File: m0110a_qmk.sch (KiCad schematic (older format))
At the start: 174 parts, among them J1 USB_B_Mini, J2 AVR-ISP-6, U1 ATmega32A-PU, Y1 Resonator

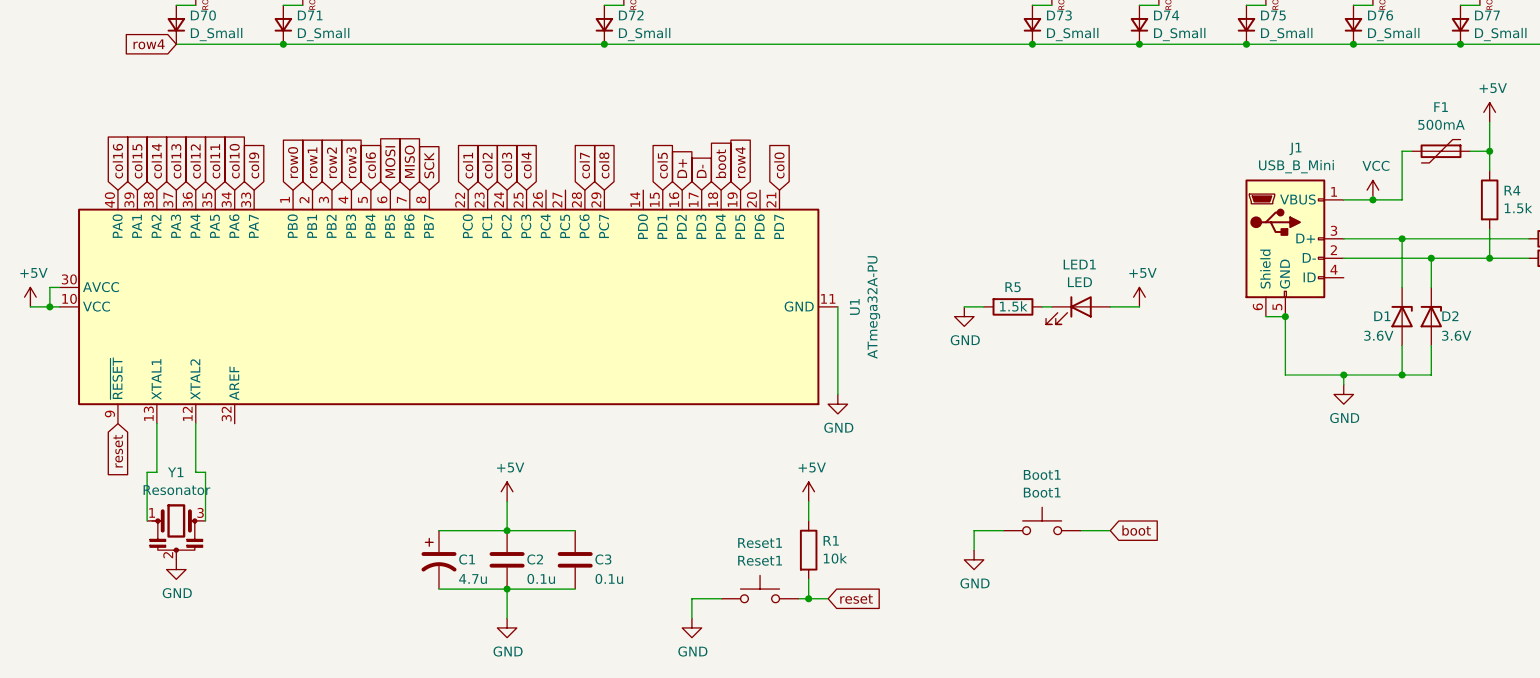
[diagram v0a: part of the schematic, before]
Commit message: change JST connector size
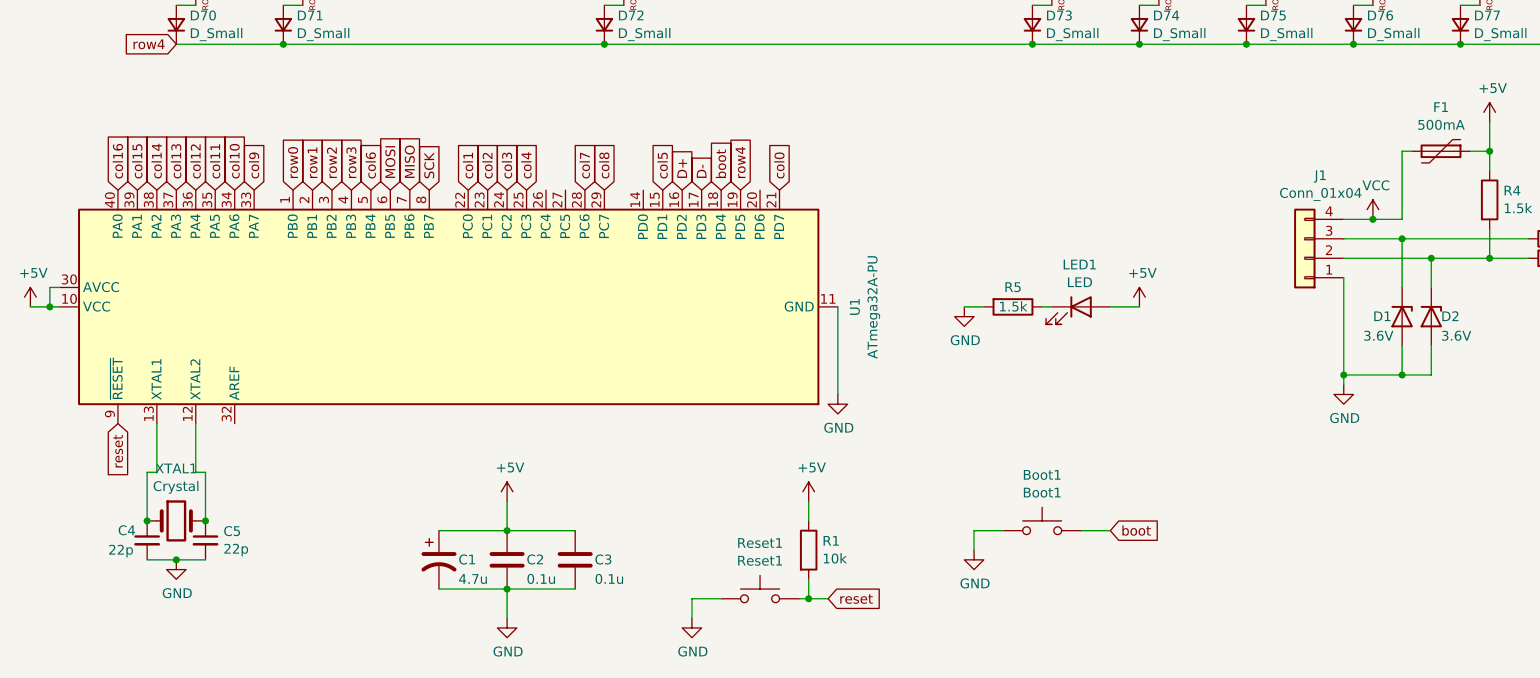
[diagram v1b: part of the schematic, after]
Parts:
- removed J1: USB_B_Mini, random-keyboard-parts:Molex-0548190519, symbol Connector:USB_B_Mini
- removed Y1: Resonator, Crystal:Resonator-3Pin_W7.0mm_H2.5mm, symbol Device:Resonator
- added C4, C5: 22p, Capacitor_THT:C_Disc_D6.0mm_W2.5mm_P5.00mm, symbol Device:C_Small
- added J1: Conn_01x04, Connector_JST:JST_PH_S4B-PH-K_1x04_P2.00mm_Horizontal, symbol Connector_Generic:Conn_01x04
- added XTAL1: Crystal, Crystal:Crystal_HC49-4H_Vertical, symbol Device:Crystal
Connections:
- net GND: now also C4.2, C5.2, J1.1 (Pin_1)
- net VCC: now also J1.4 (Pin_4)
- net at U1.12 (XTAL2): now also C5.1, XTAL1.2
- net at U1.13 (XTAL1): now also C4.1, XTAL1.1
- net at D2.1 (K), R3.1, R4.2: now also J1.2 (Pin_2)
- net at D1.1 (K), R2.1: now also J1.3 (Pin_3)
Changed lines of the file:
@@
 	0    1    1    0
 $EndComp
-Wire Wire Line
-	7700 5200 7550 5200
 $Comp
 L power:+5V #PWR01
@@
 L power:VCC #PWR03
 U 1 1 5EC6654A
-P 7550 5200
-F 0 "#PWR03" H 7550 5050 50  0001 C CNN
-F 1 "VCC" H 7567 5373 50  0000 C CNN
-F 2 "" H 7550 5200 50  0001 C CNN
-F 3 "" H 7550 5200 50  0001 C CNN
-	1    7550 5200
-	1    0    0    -1
-$EndComp
-Connection ~ 7550 5200
-Wire Wire Line
-	7550 5200 7400 5200
+P 7550 5300
+F 0 "#PWR03" H 7550 5150 50  0001 C CNN
+F 1 "VCC" H 7567 5473 50  0000 C CNN
+F 2 "" H 7550 5300 50  0001 C CNN
+F 3 "" H 7550 5300 50  0001 C CNN
+	1    7550 5300
+	1    0    0    -1
+$EndComp
 Wire Wire Line
 	7700 4950 7750 4950
@@
 Wire Wire Line
 	8150 4950 8050 4950
-$Comp
-L Connector:USB_B_Mini J1
-U 1 1 5EC7E4A9
-P 7100 5400
-F 0 "J1" H 7157 5867 50  0000 C CNN
-F 1 "USB_B_Mini" H 7157 5776 50  0000 C CNN
-F 2 "random-keyboard-parts:Molex-0548190519" H 7250 5350 50  0001 C CNN
-F 3 "~" H 7250 5350 50  0001 C CNN
-	1    7100 5400
-	1    0    0    -1
-$EndComp
-Wire Wire Line
-	7700 5200 7700 4950
 Wire Wire Line
 	8150 5050 8150 4950
-Wire Wire Line
-	7100 6100 7100 5800
 Wire Wire Line
 	7400 5400 7700 5400
@@
 	7400 6150 7400 6100
 Wire Wire Line
-	7400 6100 7100 6100
-Wire Wire Line
 	7400 6100 7700 6100
-Connection ~ 7400 6100
 Wire Wire Line
 	7700 6100 7850 6100
@@
 	8150 5500 8350 5500
 Wire Wire Line
-	7000 5800 7100 5800
-Connection ~ 7100 5800
-Wire Wire Line
 	8000 1400 8550 1400
 Wire Wire Line
@@
 Wire Wire Line
 	8000 4400 8550 4400
-$Comp
-L Device:Resonator Y1
-U 1 1 5ED6B15E
+Wire Wire Line
+	1250 6600 1250 6850
+Wire Wire Line
+	1550 6600 1550 6850
+$Comp
+L Device:Crystal XTAL1
+U 1 1 5F091829
 P 1400 6850
-F 0 "Y1" H 1400 7098 50  0000 C CNN
-F 1 "Resonator" H 1400 7007 50  0000 C CNN
-F 2 "Crystal:Resonator-3Pin_W7.0mm_H2.5mm" H 1375 6850 50  0001 C CNN
-F 3 "~" H 1375 6850 50  0001 C CNN
+F 0 "XTAL1" H 1400 7118 50  0000 C CNN
+F 1 "Crystal" H 1400 7027 50  0000 C CNN
+F 2 "Crystal:Crystal_HC49-4H_Vertical" H 1400 6850 50  0001 C CNN
+F 3 "~" H 1400 6850 50  0001 C CNN
 	1    1400 6850
 	1    0    0    -1
 $EndComp
-Wire Wire Line
-	1250 6600 1250 6850
-Wire Wire Line
-	1550 6600 1550 6850
+$Comp
+L Device:C_Small C4
+U 1 1 5F093589
+P 1250 6950
+F 0 "C4" H 1100 7000 50  0000 L CNN
+F 1 "22p" H 1050 6900 50  0000 L CNN
+F 2 "Capacitor_THT:C_Disc_D6.0mm_W2.5mm_P5.00mm" H 1250 6950 50  0001 C CNN
+F 3 "~" H 1250 6950 50  0001 C CNN
+	1    1250 6950
+	1    0    0    -1
+$EndComp
+Connection ~ 1250 6850
+$Comp
+L Device:C_Small C5
+U 1 1 5F094216
+P 1550 6950
+F 0 "C5" H 1642 6996 50  0000 L CNN
+F 1 "22p" H 1642 6905 50  0000 L CNN
+F 2 "Capacitor_THT:C_Disc_D6.0mm_W2.5mm_P5.00mm" H 1550 6950 50  0001 C CNN
+F 3 "~" H 1550 6950 50  0001 C CNN
+	1    1550 6950
+	1    0    0    -1
+$EndComp
+Connection ~ 1550 6850
+Wire Wire Line
+	1250 7050 1400 7050
+Connection ~ 1400 7050
+Wire Wire Line
+	1400 7050 1550 7050
+$Comp
+L Connector_Generic:Conn_01x04 J1
+U 1 1 5EDC2A3B
+P 7200 5500
+F 0 "J1" H 7118 5075 50  0000 C CNN
+F 1 "Conn_01x04" H 7118 5166 50  0000 C CNN
+F 2 "Connector_JST:JST_PH_S4B-PH-K_1x04_P2.00mm_Horizontal" H 7200 5500 50  0001 C CNN
+F 3 "~" H 7200 5500 50  0001 C CNN
+	1    7200 5500
+	-1   0    0    1
+$EndComp
+Wire Wire Line
+	7400 5300 7550 5300
+Wire Wire Line
+	7700 4950 7700 5300
+Connection ~ 7550 5300
+Wire Wire Line
+	7550 5300 7700 5300
+Wire Wire Line
+	7400 5600 7400 6100
+Connection ~ 7400 6100
 $EndSCHEMATC
